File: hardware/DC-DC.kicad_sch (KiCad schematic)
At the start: 10 parts, among them Q1 STL40DN3LLH5, U4 MP4247

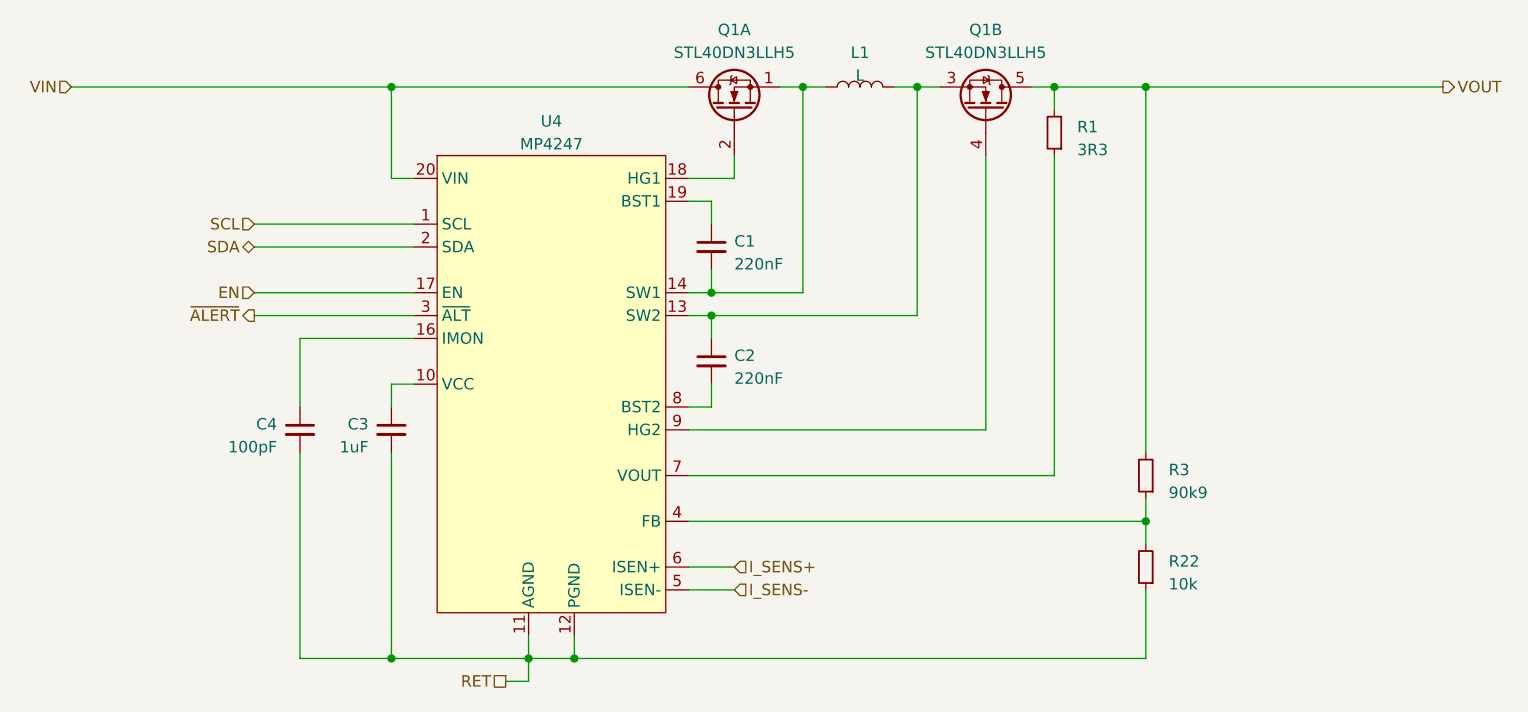
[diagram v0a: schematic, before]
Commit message: Some routing and pinout changes
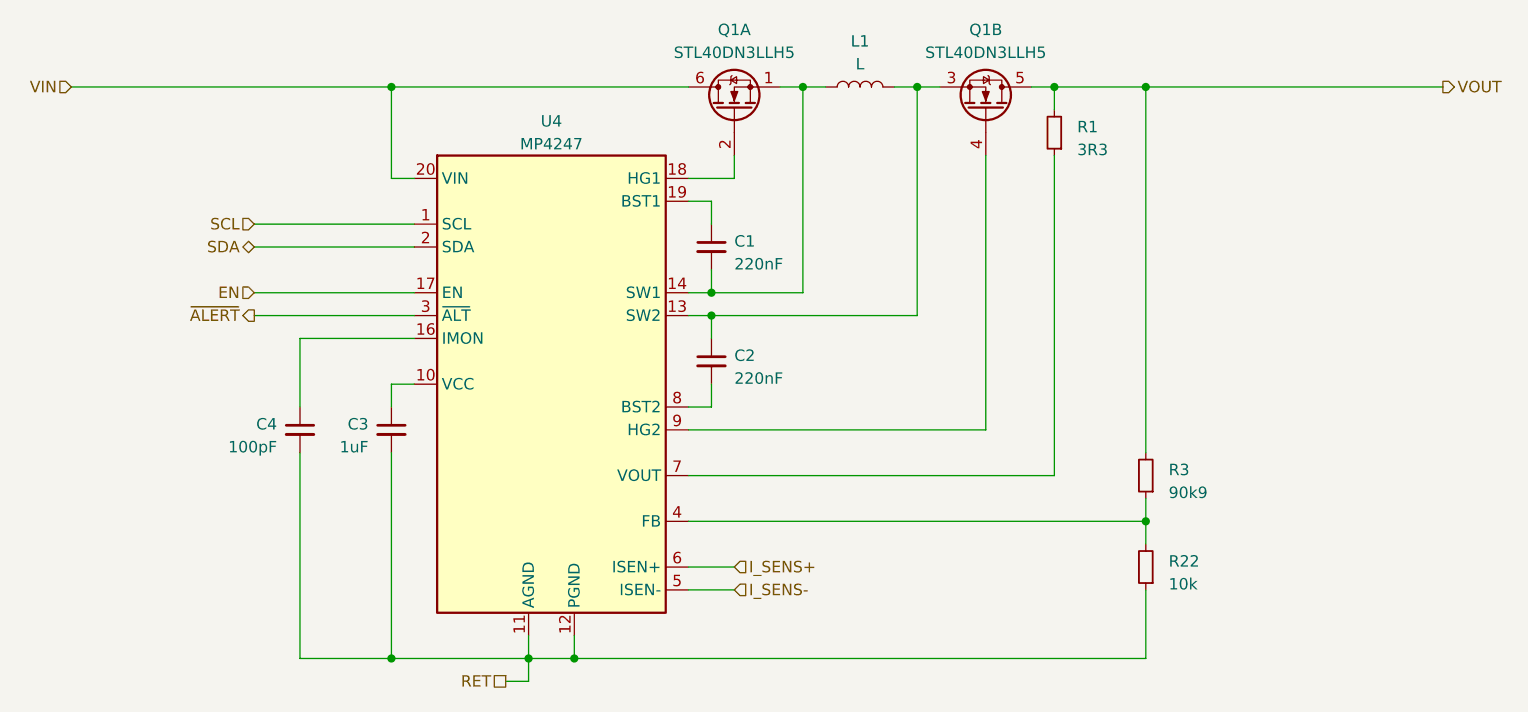
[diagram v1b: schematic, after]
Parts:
- C1, C2, C3, C4: footprint (none) -> Capacitor_SMD:C_0402_1005Metric
- Q1: footprint (none) -> Package_SON:ST_PowerFLAT-6L_5x6mm_P1.27mm
- R1: footprint (none) -> Resistor_SMD:R_0603_1608Metric
- R22, R3: footprint (none) -> Resistor_SMD:R_0402_1005Metric
- U4: footprint (none) -> Package_DFN_QFN:MPS_QFN-20_3x5mm_P0.5mm
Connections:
- net RET: now also U4.15 (PGND); no longer U4.13 (SW2)
